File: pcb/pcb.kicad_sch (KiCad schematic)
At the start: 22 parts, among them J1 AVR-ISP-6, SW1 BOOT, SW2 RESET, U1 ATmega328P-P, Y1 Crystal

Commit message: 🚧 WIP - Place the components - Wire all the components
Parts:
- removed USB1: USB_C_GCT_USB4085, Type-C:USB_C_GCT_USB4085, symbol Type-C:HRO-TYPE-C-31-M-12
- added USB1: USB_C_Receptacle_USB2.0, Type-C:USB_C_GCT_USB4085, symbol Connector:USB_C_Receptacle_USB2.0
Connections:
- net +5V: now also F1.1; no longer F1.2
- net D+: now also USB1.A6 (D+), USB1.B6 (D+)
- net D-: now also USB1.A7 (D-), USB1.B7 (D-)
- net GND: now also R1.2, R2.2, USB1.A1 (GND), USB1.A12 (GND), USB1.B1 (GND), USB1.B12 (GND), USB1.S1 (SHIELD); no longer R1.1, R2.1
- net VCC: now also F1.2, USB1.A4 (VBUS), USB1.A9 (VBUS), USB1.B4 (VBUS), USB1.B9 (VBUS); no longer F1.1
- net col0: now also U1.28 (PC5)
- net col1: now also U1.27 (PC4)
- net col10: now also U1.13 (PD7)
- net col11: now also U1.14 (PB0)
- net col2: now also U1.26 (PC3)
- net col3: now also U1.2 (PD0)
- net col4: now also U1.25 (PC2)
- net col5: now also U1.3 (PD1)
- net col6: now also U1.24 (PC1)
- net col7: now also U1.23 (PC0)
- net col8: now also U1.6 (PD4)
- net col9: now also U1.12 (PD6)
- net row2: now also U1.16 (PB2)
- net row3: now also U1.15 (PB1)
- new net: R2.1, USB1.B5 (CC2)
- new net: R1.1, USB1.A5 (CC1)

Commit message: 🏗️ Prepare for production
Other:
- title: EK_Van -> RetroVan
- moved on the sheet: C5

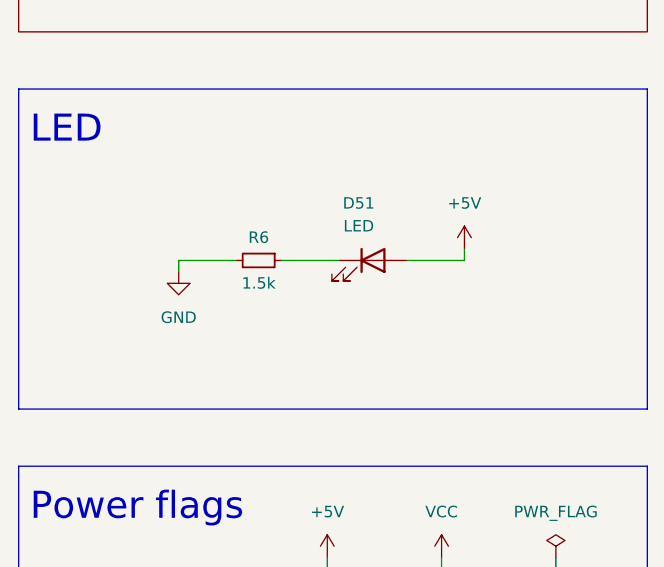
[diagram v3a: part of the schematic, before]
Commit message: 🛠️ Update LED resistor value
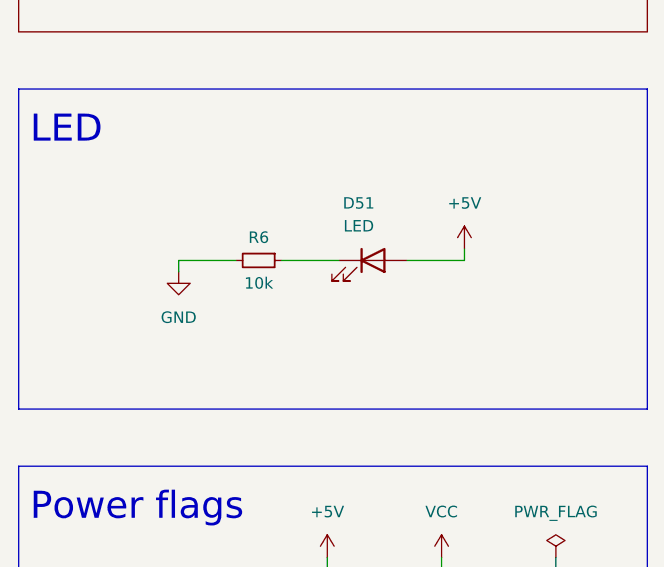
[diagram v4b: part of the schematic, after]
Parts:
- R6: value 1.5k -> 10k
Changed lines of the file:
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@@
     (in_bom yes) (on_board yes)
     (property "Reference" "R6" (id 0) (at 45.72 142.24 90))
-    (property "Value" "1.5k" (id 1) (at 45.72 147.32 90))
+    (property "Value" "10k" (id 1) (at 45.72 147.32 90))
     (property "Footprint" "Resistor_THT:R_Axial_DIN0204_L3.6mm_D1.6mm_P7.62mm_Horizontal" (id 2) (at 45.72 144.78 0)
       (effects (font (size 1.27 1.27)) hide)
@@
     )
     (path "/a16db100-1f9c-410b-a4ba-60143c88d520"
-      (reference "R6") (unit 1) (value "1.5k") (footprint "Resistor_THT:R_Axial_DIN0204_L3.6mm_D1.6mm_P7.62mm_Horizontal")
+      (reference "R6") (unit 1) (value "10k") (footprint "Resistor_THT:R_Axial_DIN0204_L3.6mm_D1.6mm_P7.62mm_Horizontal")
     )
     (path "/51cf82a7-fc50-4453-808c-b7780286c821"
